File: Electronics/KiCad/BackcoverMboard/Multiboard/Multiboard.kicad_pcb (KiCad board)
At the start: 2 copper layers, 50.8 x 40.6 mm, 8 parts, among them J1 Conn_01x05, J2 Conn_01x05_Male, J3 Conn_01x05_Male, J4 Conn_01x05, J5 USB_A, J6 USB_A, U1 FP-Back-Con

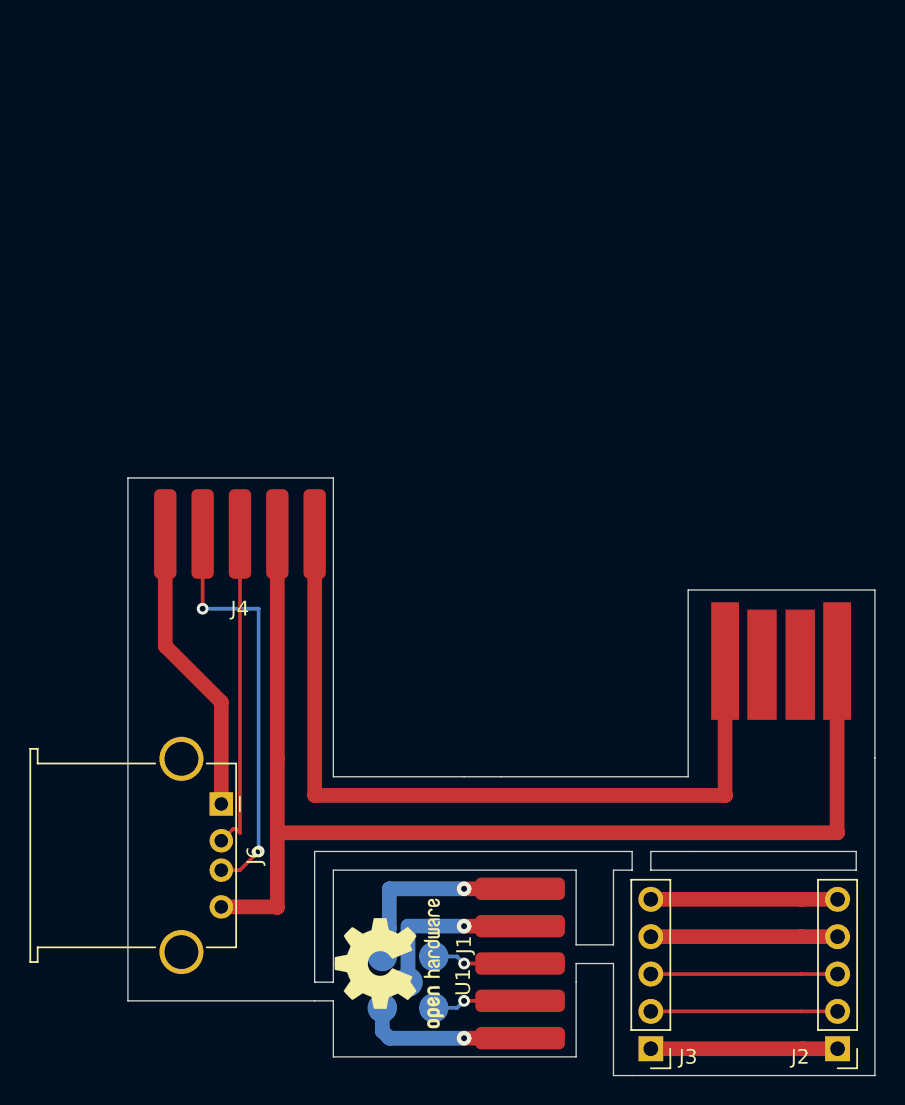
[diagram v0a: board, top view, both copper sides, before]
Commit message: added gcode and an updated board for ideal positioning of my Intenso HC 20000
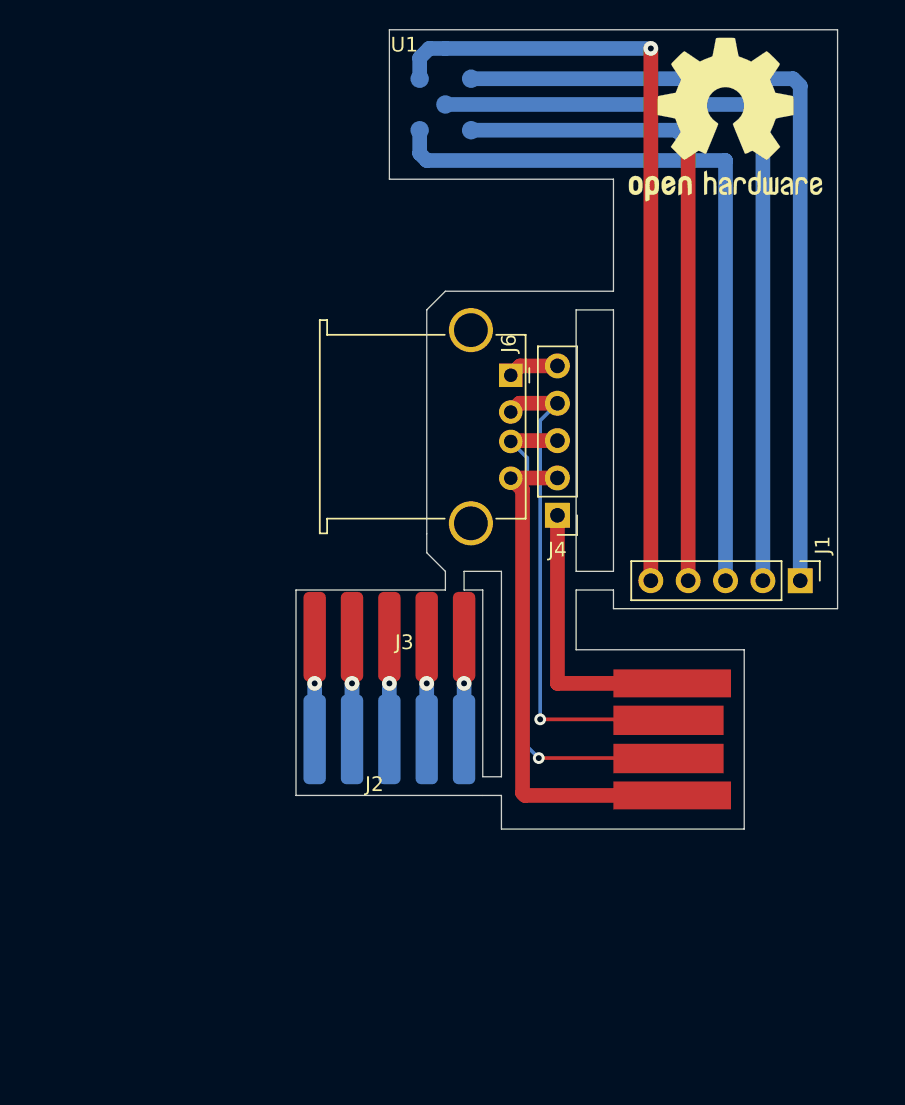
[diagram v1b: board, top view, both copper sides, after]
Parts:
- removed the REF** at (132.1, 109.2)
- added REF**: OSHW-Logo2_14.6x12mm_SilkScreen, Symbol:OSHW-Logo2_14.6x12mm_SilkScreen, F.Cu at (154.9, 51.8)
- J1, J4: footprint Fairphone-Back:Pad 01x05 -> Connector_PinHeader_2.54mm:PinHeader_1x05_P2.54mm_Vertical
- J2: footprint Connector_PinHeader_2.54mm:PinHeader_1x05_P2.54mm_Vertical -> Fairphone-Back:Pad 01x05; moved to B.Cu
- J3: footprint Connector_PinHeader_2.54mm:PinHeader_1x05_P2.54mm_Vertical -> Fairphone-Back:Pad 01x05
- moved U1 59.7 mm to (135.9, 50.8), turned to 0 degrees
- moved J2 37.0 mm to (132.1, 94.0), turned to 0 degrees
- moved J6 35.2 mm to (140.3, 69.2)
- moved J3 33.2 mm to (132.1, 87.0), turned to 0 degrees
- moved J1 32.3 mm to (160.0, 83.2)
- moved J4 21.6 mm to (143.5, 78.7)
- moved J5 10.5 mm to (156.2, 94.0), turned to 90 degrees
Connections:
- J5 pad 2: (no net) -> Net-(J4-Pad4)
- J5 pad 3: (no net) -> Net-(J4-Pad3)
- J6 pad 2: Net-(J4-Pad3) -> Net-(J4-Pad4)
- J6 pad 3: Net-(J4-Pad4) -> Net-(J4-Pad3)
- U1 pad 4: Net-(J1-Pad4) -> Net-(J1-Pad3)
- U1 pad 5: Net-(J1-Pad3) -> Net-(J1-Pad4)
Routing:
- net Net-(J1-Pad3): track 6.07 -> 51.2 mm, vias 1 -> 0
- net Net-(J4-Pad2): track 79.0 -> 35.2 mm
- net Net-(J1-Pad1): track 13.7 -> 56.2 mm, vias 1 -> 0
- net Net-(J1-Pad2): track 11.4 -> 54.0 mm, vias 1 -> 0
- net Net-(J1-Pad5): track 11.1 -> 53.6 mm
- net Net-(J1-Pad4): track 6.07 -> 44.9 mm
- net Net-(J4-Pad1): track 54.9 -> 19.2 mm
- net Net-(J4-Pad5): track 19.9 -> 3.44 mm
- net Net-(J4-Pad3): track 22.0 -> 34.3 mm, vias 0 -> 1
- net Net-(J2-Pad5): track 12.7 -> 6.98 mm, vias 0 -> 1
- net Net-(J2-Pad4): track 12.7 -> 6.98 mm, vias 0 -> 1
- net Net-(J2-Pad3): track 12.7 -> 6.98 mm, vias 0 -> 1
- net Net-(J2-Pad2): track 12.7 -> 6.98 mm, vias 0 -> 1
- net Net-(J2-Pad1): track 12.7 -> 6.98 mm, vias 0 -> 1
- net Net-(J4-Pad4): track 28.5 -> 34.1 mm, vias 2 -> 1
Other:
- board size 50.8 x 40.6 mm -> 36.8 x 54.4 mm
